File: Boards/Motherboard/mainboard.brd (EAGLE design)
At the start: 62.2 x 63.2 mm, 15 parts, among them IC1 7805TV

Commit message: * Changed the rotary encoder code, to match that of the following source:    - https://www.instructables.com/Tutorial-of-Rotary-Encoder-With-Arduino/ * Changed boards and schematic, so that interrupt pins are correct
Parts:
- moved MOTOR_B 17.8 mm to (52.1, 34.3)
- moved DIGITAL_B 8.89 mm to (52.1, 25.4)
- moved DIGITAL_A 8.89 mm to (52.1, 16.5)
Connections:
- removed net D2: DIGITAL.5, DIGITAL_C.1
- removed net D3: DIGITAL.6, DIGITAL_B.1
- new net D7: DIGITAL.10, DIGITAL_B.1
- new net D8: DIGITAL.11, DIGITAL_A.1
- net D4: now also DIGITAL_C.1; no longer DIGITAL_A.1
- net D5: now also MOTOR_B.1; no longer MOTOR_B.2
- net D6: now also MOTOR_B.2; no longer MOTOR_B.1
- net REB_A: now also FRONT_PANEL.3; no longer FRONT_PANEL.4
- net REB_B: now also DIGITAL.5, FRONT_PANEL.5; no longer DIGITAL.15, FRONT_PANEL.3
- net REB_SWITCH: now also DIGITAL.6, FRONT_PANEL.4; no longer DIGITAL.11, FRONT_PANEL.5
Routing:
- net REB_SWITCH: track 67.7 -> 48.8 mm
- net REB_B: track 67.3 -> 50.7 mm
- net D2: track 13.8 -> 0.00 mm
- net D8: track 0.00 -> 11.7 mm
- net D7: track 0.00 -> 11.2 mm
- net D3: track 11.0 -> 0.00 mm
- net D4: track 12.4 -> 18.4 mm
- net REB_A: track 70.5 -> 65.5 mm
- net D5: track 18.6 -> 14.3 mm
- net D6: track 14.7 -> 17.9 mm
- net RXD: track 14.0 -> 16.1 mm
- net TXD: track 18.1 -> 20.0 mm
- net A7: track 13.0 -> 14.3 mm
- net +12V: track 123.4 -> 122.3 mm

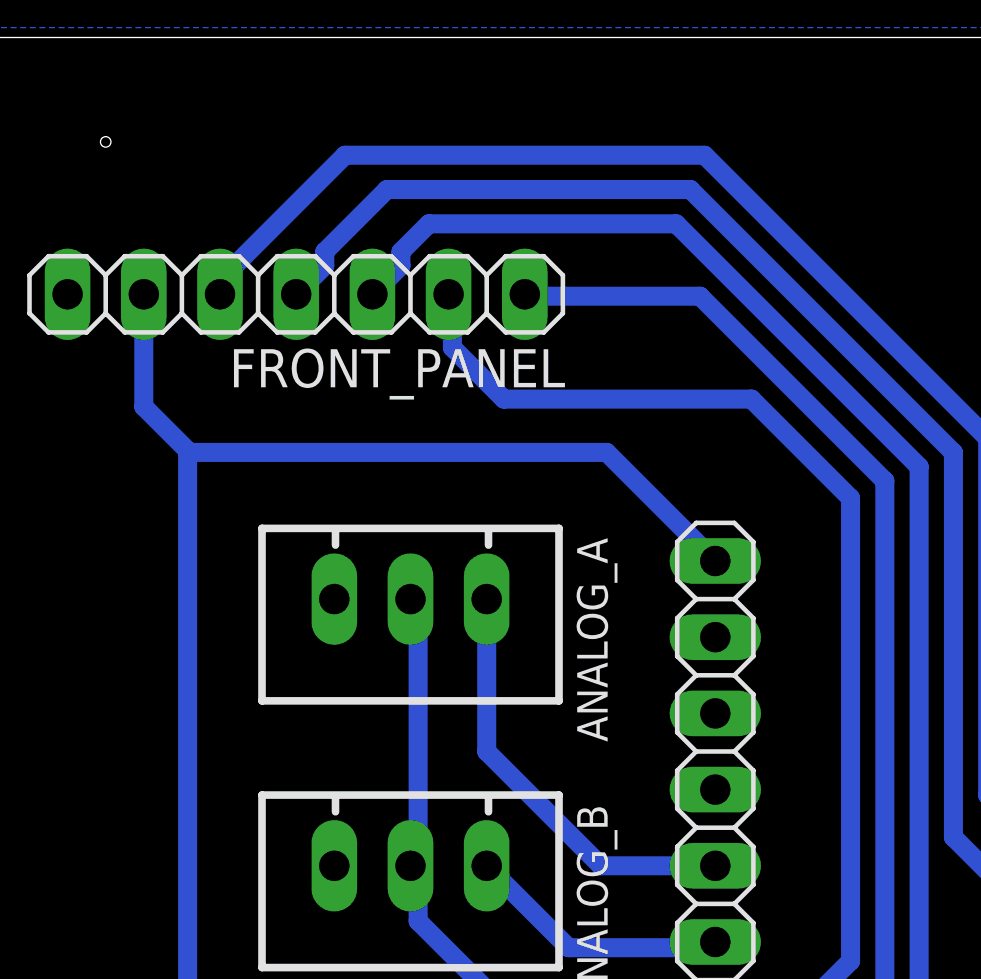
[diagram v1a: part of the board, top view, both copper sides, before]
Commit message: * Made some minor changes on the motherboard, so that the +5v rail is connected to +5v on the arduino instead of vin
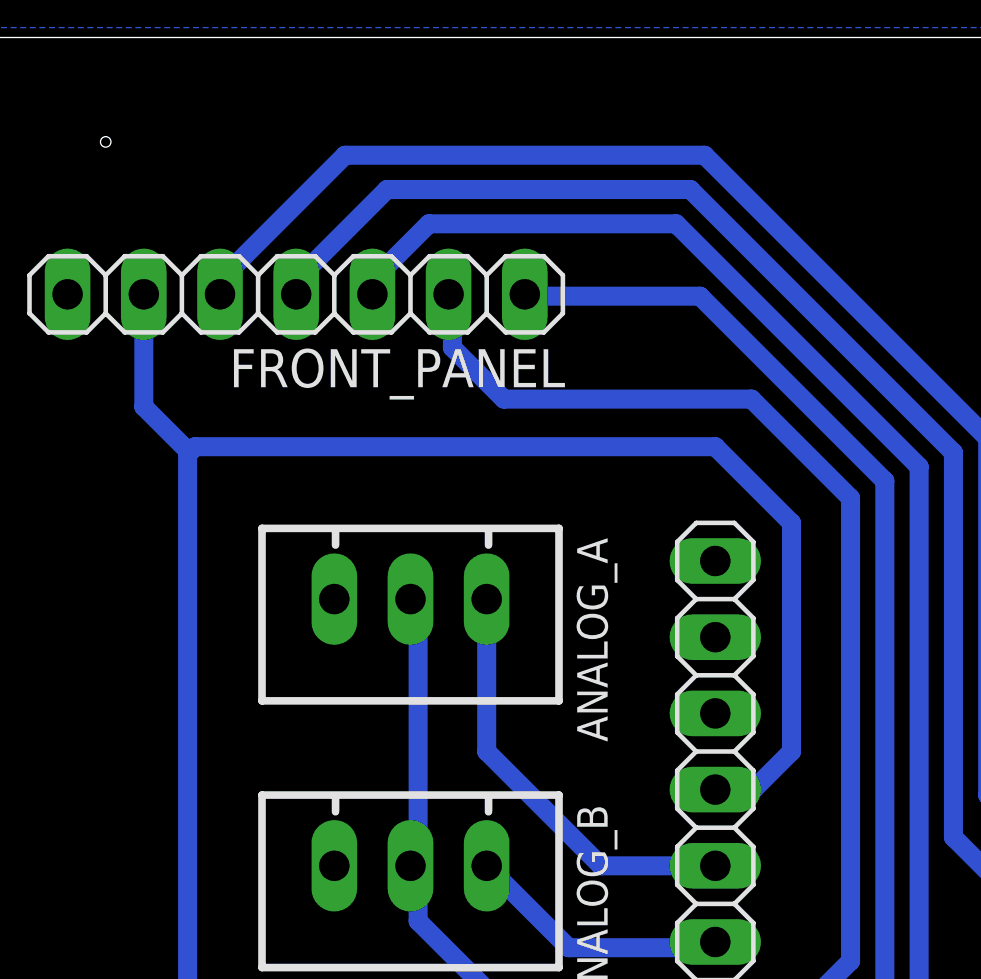
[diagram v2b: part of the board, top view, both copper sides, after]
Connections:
- net +5V: now also ANALOG.12; no longer ANALOG.15
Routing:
- net +5V: track 59.0 -> 71.8 mm
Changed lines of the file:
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@@
 <signal name="+5V">
 <contactref element="IC1" pad="3"/>
-<contactref element="ANALOG" pad="15"/>
 <contactref element="FRONT_PANEL" pad="6"/>
 <wire x1="10.922" y1="17.9705" x2="11.3665" y2="17.9705" width="0.635" layer="16"/>
@@
 <wire x1="6.5405" y1="49.3395" x2="6.5405" y2="27.7095" width="0.635" layer="16"/>
 <wire x1="8.85" y1="25.4" x2="6.5405" y2="27.7095" width="0.635" layer="16"/>
-<wire x1="24.13" y1="45.72" x2="20.5105" y2="49.3395" width="0.635" layer="16"/>
-<wire x1="20.5105" y1="49.3395" x2="6.604" y2="49.3395" width="0.635" layer="16"/>
 <wire x1="6.604" y1="49.3395" x2="6.5405" y2="49.3395" width="0.635" layer="16"/>
 <contactref element="C4" pad="+"/>
 <wire x1="8.85" y1="25.4" x2="9.0805" y2="25.4" width="0.635" layer="16"/>
+<contactref element="ANALOG" pad="12"/>
+<wire x1="24.13" y1="38.1" x2="25.4" y2="38.1" width="0.635" layer="16"/>
+<wire x1="25.4" y1="38.1" x2="26.67" y2="39.37" width="0.635" layer="16"/>
+<wire x1="26.67" y1="46.99" x2="24.13" y2="49.53" width="0.635" layer="16"/>
+<wire x1="6.7945" y1="49.53" x2="6.604" y2="49.3395" width="0.635" layer="16"/>
+<wire x1="26.67" y1="39.37" x2="26.67" y2="46.99" width="0.635" layer="16"/>
+<wire x1="24.13" y1="49.53" x2="6.7945" y2="49.53" width="0.635" layer="16"/>
 </signal>
 <signal name="D4">
@@
 <contactref element="DIGITAL" pad="14"/>
 <contactref element="FRONT_PANEL" pad="3"/>
-<wire x1="13.6525" y1="56.02956875" x2="14.58243125" y2="56.9595" width="0.635" layer="16"/>
-<wire x1="12.7" y1="54.61" x2="13.6525" y2="55.5625" width="0.635" layer="16"/>
-<wire x1="13.6525" y1="55.5625" x2="13.6525" y2="56.02956875" width="0.635" layer="16"/>
+<wire x1="14.58243125" y1="56.9595" x2="12.7" y2="55.07706875" width="0.635" layer="16"/>
+<wire x1="12.7" y1="54.61" x2="12.7" y2="55.07706875" width="0.635" layer="16"/>
 <wire x1="14.58243125" y1="56.9595" x2="22.82545" y2="56.9595" width="0.635" layer="16"/>
 <wire x1="22.82545" y1="56.9595" x2="30.9245" y2="48.86045" width="0.635" layer="16"/>
@@
 <wire x1="35.56" y1="33.02" x2="32.0675" y2="36.5125" width="0.635" layer="16"/>
 <wire x1="32.0675" y1="49.3339" x2="23.2989" y2="58.1025" width="0.635" layer="16"/>
-<wire x1="11.1125" y1="56.02956875" x2="11.1125" y2="55.5625" width="0.635" layer="16"/>
-<wire x1="11.1125" y1="55.5625" x2="10.16" y2="54.61" width="0.635" layer="16"/>
-<wire x1="13.18543125" y1="58.1025" x2="11.1125" y2="56.02956875" width="0.635" layer="16"/>
+<wire x1="13.18543125" y1="58.1025" x2="10.16" y2="55.07706875" width="0.635" layer="16"/>
+<wire x1="10.16" y1="55.07706875" x2="10.16" y2="54.61" width="0.635" layer="16"/>
 <wire x1="32.0675" y1="36.5125" x2="32.0675" y2="49.3339" width="0.635" layer="16"/>
 <wire x1="23.2989" y1="58.1025" x2="13.18543125" y2="58.1025" width="0.635" layer="16"/>

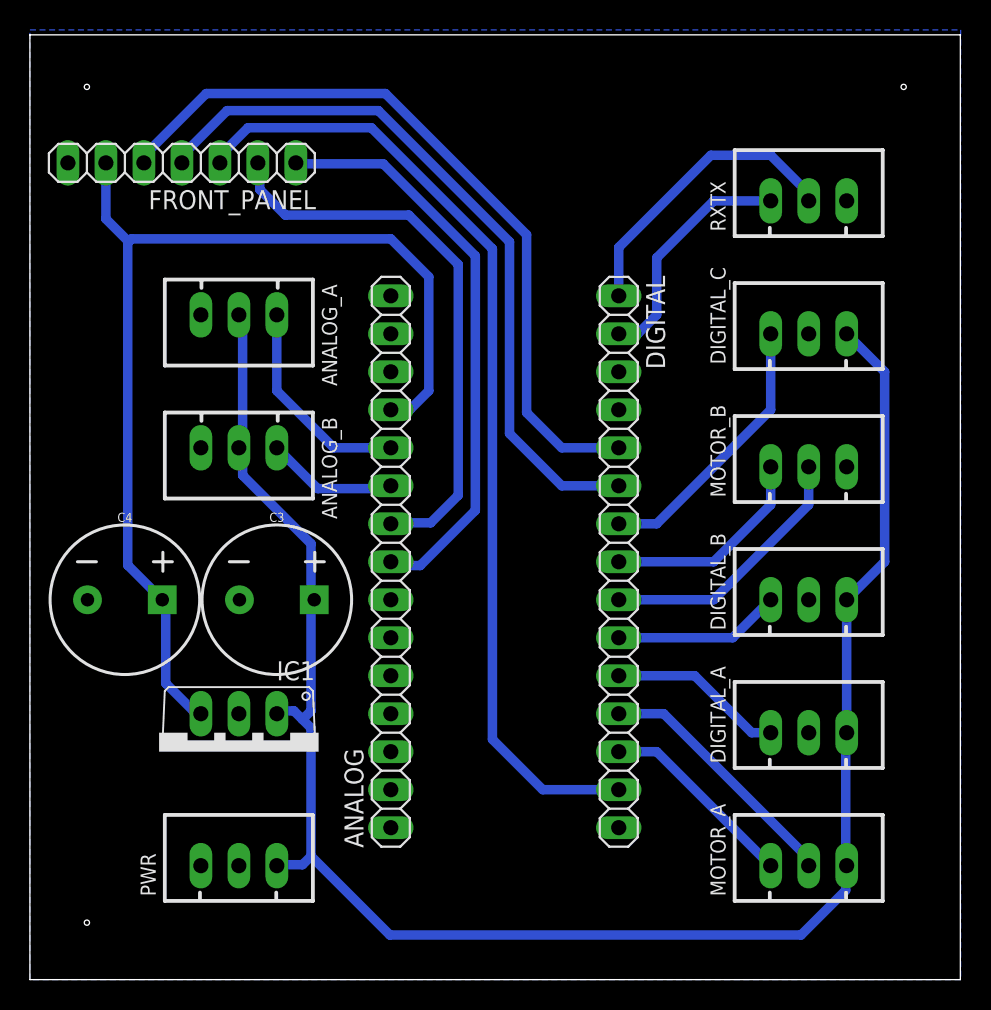
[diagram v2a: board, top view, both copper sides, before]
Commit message: * Optimised the motherboard a little
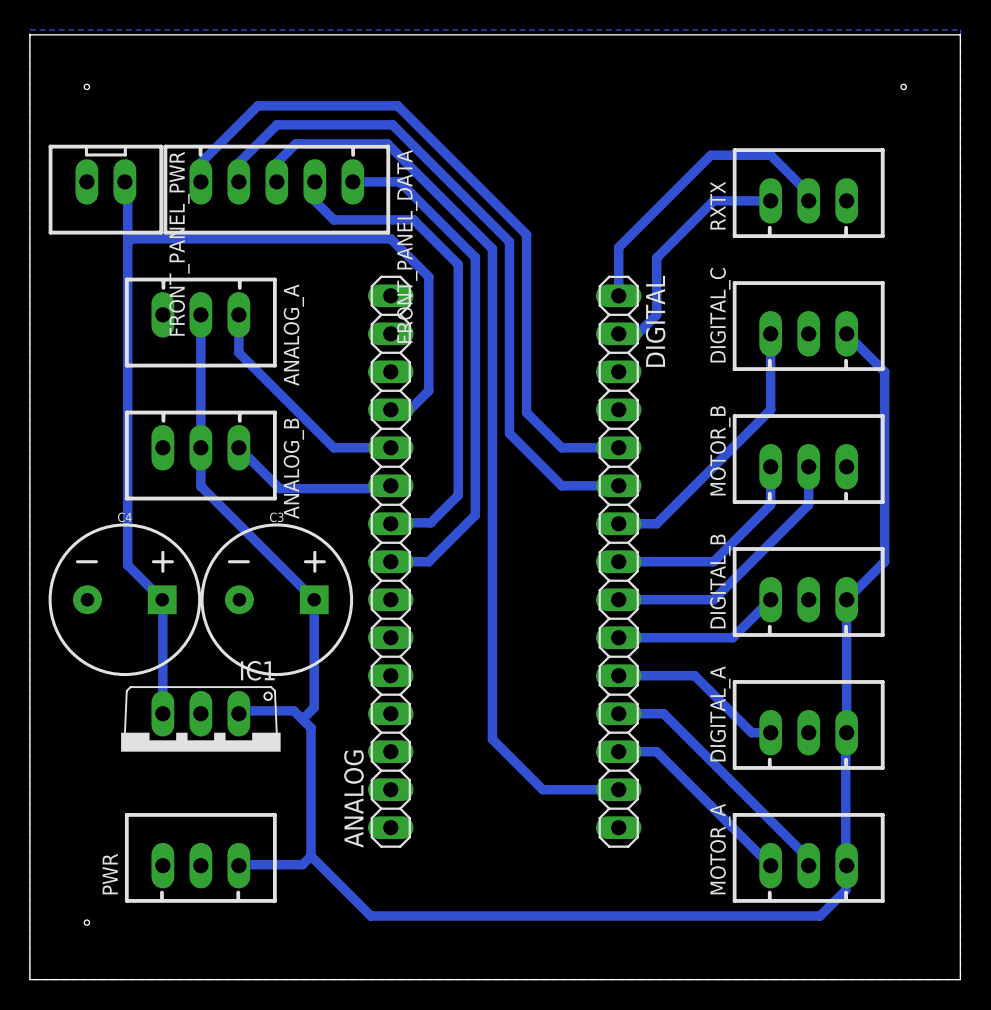
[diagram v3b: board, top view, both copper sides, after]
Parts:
- removed FRONT_PANEL: (no value), pinhead:1X07
- added FRONT_PANEL_DATA: JST-XH-05-PIN-LONG-PAD, Rembrandt Electronics - JST XH Connectors v1-0:JST-XH-05-PACKAGE-LONG-PAD
- added FRONT_PANEL_PWR: JST-XH-02-PIN-LONG-PAD, Rembrandt Electronics - JST XH Connectors v1-0:JST-XH-02-PACKAGE-LONG-PAD
- moved ANALOG_A 2.54 mm to (11.4, 44.5)
- moved ANALOG_B 2.54 mm to (11.4, 35.6)
- moved IC1 2.54 mm to (11.4, 15.2)
- moved PWR 2.54 mm to (11.4, 7.62)
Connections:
- net +5V: now also FRONT_PANEL_PWR.1; no longer FRONT_PANEL.6
- net GND: now also FRONT_PANEL_PWR.2; no longer FRONT_PANEL.7
- net REB_A: now also FRONT_PANEL_DATA.3; no longer FRONT_PANEL.3
- net REB_B: now also FRONT_PANEL_DATA.5; no longer FRONT_PANEL.5
- net REB_SWITCH: now also FRONT_PANEL_DATA.4; no longer FRONT_PANEL.4
- net SCL: now also FRONT_PANEL_DATA.2; no longer FRONT_PANEL.2
- net SDA: now also FRONT_PANEL_DATA.1; no longer FRONT_PANEL.1
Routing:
- net +12V: track 122.3 -> 127.2 mm
- net SCL: track 37.9 -> 33.3 mm
- net SDA: track 38.8 -> 34.5 mm
- net REB_A: track 65.5 -> 61.8 mm
- net REB_SWITCH: track 48.8 -> 45.2 mm
- net REB_B: track 50.7 -> 47.2 mm
- net +5V: track 71.8 -> 68.8 mm
- net A6: track 8.83 -> 11.4 mm
- net A7: track 14.3 -> 15.3 mm
